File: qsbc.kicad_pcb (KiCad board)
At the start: 6 copper layers, 80 x 80 mm, 2 parts, among them U1 MIMX8MM6DVTLZAA, U3 MT40A1G16KD-062E

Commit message: misc work, usb sch done
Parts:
- added C1: 0.22uF, Capacitor_SMD:C_0201_0603Metric, F.Cu at (119.7, 123.8)
- added C10: 4.7uF, Capacitor_SMD:C_0402_1005Metric, F.Cu at (122.8, 121.9)
- added C11: 4.7uF, Capacitor_SMD:C_0402_1005Metric, F.Cu at (125.6, 121.7)
- added C12: 0.01uF, Capacitor_SMD:C_0201_0603Metric, F.Cu at (134.4, 115.7)
- added C13: 2.2uF, Capacitor_SMD:C_0402_1005Metric, F.Cu at (81.5, 124.2)
- added C14: 2.2uF, Capacitor_SMD:C_0402_1005Metric, F.Cu at (97.5, 112.0)
- added C15: 2.2uF, Capacitor_SMD:C_0402_1005Metric, F.Cu at (78.7, 124.0)
- added C16: 4.7uF, Capacitor_SMD:C_0402_1005Metric, F.Cu at (90.8, 120.1)
- added C17: 4.7uF, Capacitor_SMD:C_0402_1005Metric, F.Cu at (90.7, 122.1)
- added C18: 4.7uF, Capacitor_SMD:C_0402_1005Metric, F.Cu at (93.9, 115.1)
- added C2: 4.7uF, Capacitor_SMD:C_0402_1005Metric, F.Cu at (125.6, 123.7)
- added C27: 1uF, Capacitor_SMD:C_0402_1005Metric, F.Cu at (90.1, 124.0)
- added C28: 1uF, Capacitor_SMD:C_0402_1005Metric, F.Cu at (97.5, 114.0)
- added C29: 4.7uF, Capacitor_SMD:C_0402_1005Metric, F.Cu at (96.8, 116.0)
- added C3: 4.7uF, Capacitor_SMD:C_0402_1005Metric, F.Cu at (131.7, 115.8)
- added C30: 4.7uF, Capacitor_SMD:C_0402_1005Metric, F.Cu at (87.3, 124.2)
- added C31: 4.7uF, Capacitor_SMD:C_0402_1005Metric, F.Cu at (87.8, 121.2)
- added C32: 4.7uF, Capacitor_SMD:C_0402_1005Metric, F.Cu at (93.7, 119.0)
- added C4: 4.7uF, Capacitor_SMD:C_0402_1005Metric, F.Cu at (131.7, 117.8)
- added C45: 18pF, Capacitor_SMD:C_0402_1005Metric, F.Cu at (100.4, 112.0)
- added C47: 18pF, Capacitor_SMD:C_0402_1005Metric, F.Cu at (93.9, 117.0)
- added C48: 1uF, Capacitor_SMD:C_0402_1005Metric, F.Cu at (90.8, 118.1)
- added C49: 1uF, Capacitor_SMD:C_0402_1005Metric, F.Cu at (84.4, 124.2)
- added C5: 4.7uF, Capacitor_SMD:C_0402_1005Metric, F.Cu at (126.0, 117.8)
- added C50: 0.1uF, Capacitor_SMD:C_0402_1005Metric, F.Cu at (144.6, 173.0)
- added C51: 0.1uF, Capacitor_SMD:C_0402_1005Metric, F.Cu at (154.0, 167.7)
- added C52: 1nF, Capacitor_SMD:C_0603_1608Metric, F.Cu at (150.5, 168.0)
- added C53: 0.1uF, Capacitor_SMD:C_0402_1005Metric, F.Cu at (155.3, 164.5)
- added C54: 10uF, Capacitor_SMD:C_0603_1608Metric, F.Cu at (136.4, 173.3)
- added C6: 1uF, Capacitor_SMD:C_0402_1005Metric, F.Cu at (128.9, 115.8)
- added C7: 1uF, Capacitor_SMD:C_0402_1005Metric, F.Cu at (128.7, 119.7)
- added C8: 4.7uF, Capacitor_SMD:C_0402_1005Metric, F.Cu at (125.8, 119.7)
- added C9: 4.7uF, Capacitor_SMD:C_0402_1005Metric, F.Cu at (128.8, 117.8)
- added FB1: FerriteBead, Resistor_SMD:R_0603_1608Metric, F.Cu at (140.4, 173.2)
- added J1: USB_C_Receptacle_USB2.0, Connector_USB:USB_C_Receptacle_HRO_TYPE-C-31-M-12, F.Cu at (136.1, 65.1)
- added J2: USB_C_Receptacle_USB2.0, Connector_USB:USB_C_Receptacle_HRO_TYPE-C-31-M-12, F.Cu at (135.3, 132.8)
- added J3: USB_C_Receptacle_USB2.0, Connector_USB:USB_C_Receptacle_HRO_TYPE-C-31-M-12, F.Cu at (153.2, 132.5)
- added J4: ARJM11D7-502-AB-EW2, qsbc:ARJM11D7-502-AB-EW2, F.Cu at (175.9, 119.7)
- added J7: USB_C_Receptacle_USB2.0, Connector_USB:USB_C_Receptacle_HRO_TYPE-C-31-M-12, F.Cu at (117.3, 133.2)
- added R12: 100K, Resistor_SMD:R_0402_1005Metric, F.Cu at (138.8, 175.5)
- added R13: 100K, Resistor_SMD:R_0402_1005Metric, F.Cu at (150.0, 170.2)
- added R14: 100K, Resistor_SMD:R_0402_1005Metric, F.Cu at (135.9, 175.5)
- added R17: 30K, Resistor_SMD:R_0402_1005Metric, F.Cu at (155.3, 162.5)
- added R18: 1M, Resistor_SMD:R_0402_1005Metric, F.Cu at (141.7, 175.5)
- added R3: 43R, Resistor_SMD:R_0201_0603Metric, F.Cu at (122.6, 123.7)
- added R4: 43R, Resistor_SMD:R_0201_0603Metric, F.Cu at (131.3, 119.6)
- added R5: 43R, Resistor_SMD:R_0201_0603Metric, F.Cu at (128.3, 121.6)
- added R6: 10K, Resistor_SMD:R_0402_1005Metric, F.Cu at (119.9, 121.9)
- added R7: 1K, Resistor_SMD:R_0402_1005Metric, F.Cu at (126.0, 115.8)
- added R8: 1K, Resistor_SMD:R_0402_1005Metric, F.Cu at (122.9, 118.8)
- added TP1: TestPoint, TestPoint:TestPoint_Pad_D1.0mm, F.Cu at (120.0, 116.3)
- added TP10: TestPoint, TestPoint:TestPoint_Pad_D1.0mm, F.Cu at (82.4, 112.6)
- added TP11: TestPoint, TestPoint:TestPoint_Pad_D1.0mm, F.Cu at (84.8, 115.6)
- added TP12: TestPoint, TestPoint:TestPoint_Pad_D1.0mm, F.Cu at (85.4, 112.6)
- added TP13: TestPoint, TestPoint:TestPoint_Pad_D1.0mm, F.Cu at (84.8, 118.7)
- added TP14: TestPoint, TestPoint:TestPoint_Pad_D1.0mm, F.Cu at (78.7, 118.5)
- added TP15: TestPoint, TestPoint:TestPoint_Pad_D1.0mm, F.Cu at (78.7, 115.4)
- added TP16: TestPoint, TestPoint:TestPoint_Pad_D1.0mm, F.Cu at (84.8, 121.7)
- added TP17: TestPoint, TestPoint:TestPoint_Pad_D1.0mm, F.Cu at (87.9, 118.7)
- added TP18: TestPoint, TestPoint:TestPoint_Pad_D1.0mm, F.Cu at (87.9, 115.6)
- added TP19: TestPoint, TestPoint:TestPoint_Pad_D1.0mm, F.Cu at (78.7, 121.5)
- added TP2: TestPoint, TestPoint:TestPoint_Pad_D1.0mm, F.Cu at (120.0, 119.4)
- added TP20: TestPoint, TestPoint:TestPoint_Pad_D1.0mm, F.Cu at (88.5, 112.6)
- added TP3: TestPoint, TestPoint:TestPoint_Pad_D1.0mm, F.Cu at (123.0, 116.3)
- added TP4: TestPoint, TestPoint:TestPoint_Pad_D1.0mm, F.Cu at (94.6, 112.6)
- added TP5: TestPoint, TestPoint:TestPoint_Pad_D1.0mm, F.Cu at (90.9, 115.6)
- added TP6: TestPoint, TestPoint:TestPoint_Pad_D1.0mm, F.Cu at (91.5, 112.6)
- added TP7: TestPoint, TestPoint:TestPoint_Pad_D1.0mm, F.Cu at (81.8, 115.6)
- added TP8: TestPoint, TestPoint:TestPoint_Pad_D1.0mm, F.Cu at (81.8, 121.7)
- added TP9: TestPoint, TestPoint:TestPoint_Pad_D1.0mm, F.Cu at (81.8, 118.7)
- added U10: TUSB320LI, Package_DFN_QFN:Texas_X2QFN-12_1.6x1.6mm_P0.4mm, F.Cu at (138.3, 151.9)
- added U11: TUSB320, Package_DFN_QFN:Texas_X2QFN-12_1.6x1.6mm_P0.4mm, F.Cu at (142.1, 151.9)
- added U12: TPD4EUSB30, Package_SON:USON-10_2.5x1.0mm_P0.5mm, F.Cu at (132.1, 152.0)
- added U13: TPD4EUSB30, Package_SON:USON-10_2.5x1.0mm_P0.5mm, F.Cu at (178.2, 112.0)
- added U14: TPD4EUSB30, Package_SON:USON-10_2.5x1.0mm_P0.5mm, F.Cu at (174.2, 112.0)
- added U15: W25Q32JVZP, Package_SON:WSON-8-1EP_6x5mm_P1.27mm_EP3.4x4.3mm, F.Cu at (167.0, 81.8)
- added U16: BD71847MWV, qsbc:UQFN56BV7070, F.Cu at (119.5, 114.7)
- added U17: CH343P, Package_DFN_QFN:QFN-16-1EP_3x3mm_P0.5mm_EP1.45x1.45mm_ThermalVias, F.Cu at (116.2, 130.1)
- added U18: RTL8211F, Package_DFN_QFN:QFN-40-1EP_5x5mm_P0.4mm_EP3.6x3.6mm_ThermalVias, F.Cu at (172.1, 105.2)
- added U19: NX5P3363, Package_CSP:WLCSP-16_2.225x2.17mm_P0.5mm, F.Cu at (151.2, 164.1)
- added U4: TPD4EUSB30, Package_SON:USON-10_2.5x1.0mm_P0.5mm, F.Cu at (133.0, 174.0)
- added U5: CH343P, Package_DFN_QFN:QFN-16-1EP_3x3mm_P0.5mm_EP1.45x1.45mm_ThermalVias, F.Cu at (145.9, 169.4)
- added U7: TPD4EUSB30, Package_SON:USON-10_2.5x1.0mm_P0.5mm, F.Cu at (134.9, 152.0)
- added U9: NX5P3363, Package_CSP:WLCSP-16_2.225x2.17mm_P0.5mm, F.Cu at (145.9, 164.1)
- added Y1: Crystal, Crystal:Crystal_SMD_2012-2Pin_2.0x1.2mm, F.Cu at (79.0, 112.5)
- moved U3 37.6 mm to (125.5, 105.9)
- moved U1 33.4 mm to (147.9, 98.9)
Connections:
- U1 pad A22: unconnected-(U1-PadA22) -> /USB/USB1_DN
- U1 pad A23: unconnected-(U1-PadA23) -> /USB/USB2_DN
- U1 pad B22: unconnected-(U1-PadB22) -> /USB/USB1_DP
- U1 pad B23: unconnected-(U1-PadB23) -> /USB/USB2_DP
- U1 pad D22: unconnected-(U1-PadD22) -> /USB/USB1_ID
- U1 pad D23: unconnected-(U1-PadD23) -> /USB/USB2_ID
- U1 pad P1: /DDR/DRAM_VREF -> /DDR/PHY_VREF
- U3 pad A2: unconnected-(U3-PadA2) -> GND
- U3 pad A8: unconnected-(U3-PadA8) -> GND
- U3 pad B2: unconnected-(U3-PadB2) -> GND
- U3 pad C9: unconnected-(U3-PadC9) -> GND
- U3 pad D2: unconnected-(U3-PadD2) -> GND
- U3 pad D8: unconnected-(U3-PadD8) -> GND
- U3 pad E1: unconnected-(U3-PadE1) -> GND
- U3 pad E3: unconnected-(U3-PadE3) -> GND
- U3 pad E8: unconnected-(U3-PadE8) -> GND
- U3 pad E9: unconnected-(U3-PadE9) -> GND
- U3 pad F1: unconnected-(U3-PadF1) -> GND
- U3 pad G8: unconnected-(U3-PadG8) -> GND
- U3 pad H1: unconnected-(U3-PadH1) -> GND
- U3 pad H9: unconnected-(U3-PadH9) -> GND
- U3 pad K1: unconnected-(U3-PadK1) -> GND
- U3 pad K9: unconnected-(U3-PadK9) -> GND
- U3 pad M9: unconnected-(U3-PadM9) -> GND
- U3 pad N1: unconnected-(U3-PadN1) -> GND
- U3 pad T1: unconnected-(U3-PadT1) -> GND
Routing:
- net /DDR/DRAM_A13: track 0.00 -> 3.56 mm
- net /DDR/DRAM_A10: track 0.00 -> 2.77 mm

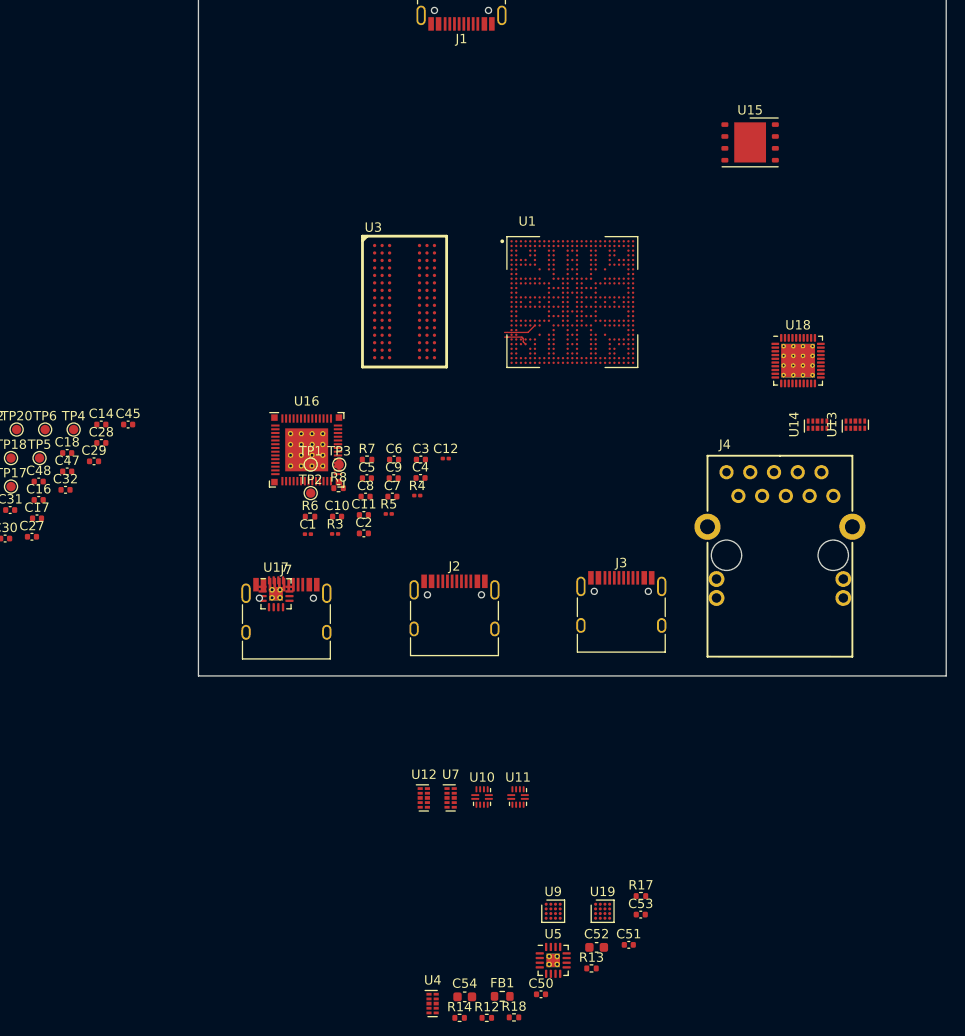
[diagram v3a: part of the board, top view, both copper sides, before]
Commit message: enet sch done, other misc sch work
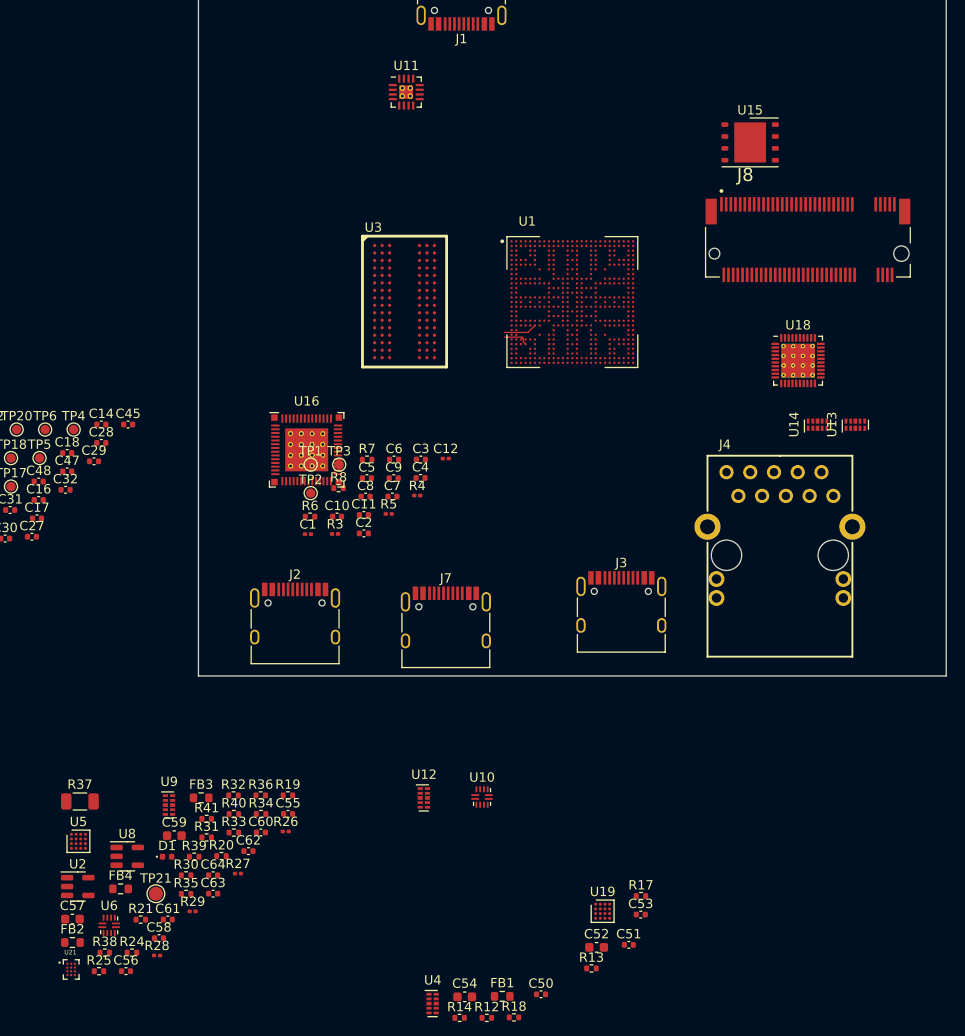
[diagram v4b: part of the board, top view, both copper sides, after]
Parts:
- removed U17: CH343P, Package_DFN_QFN:QFN-16-1EP_3x3mm_P0.5mm_EP1.45x1.45mm_ThermalVias
- removed U7: TPD4EUSB30, Package_SON:USON-10_2.5x1.0mm_P0.5mm
- added C55: 0.1uF, Capacitor_SMD:C_0402_1005Metric, F.Cu at (117.5, 153.7)
- added C56: 0.1uF, Capacitor_SMD:C_0402_1005Metric, F.Cu at (100.2, 170.5)
- added C57: 1nF, Capacitor_SMD:C_0603_1608Metric, F.Cu at (94.5, 164.9)
- added C58: 0.1uF, Capacitor_SMD:C_0402_1005Metric, F.Cu at (103.7, 167.0)
- added C59: 10uF, Capacitor_SMD:C_0603_1608Metric, F.Cu at (105.4, 156.0)
- added C60: 0.22uF, Capacitor_SMD:C_0402_1005Metric, F.Cu at (114.6, 155.7)
- added C61: 0.22uF, Capacitor_SMD:C_0402_1005Metric, F.Cu at (104.7, 165.0)
- added C62: 1uF, Capacitor_SMD:C_0402_1005Metric, F.Cu at (113.3, 157.7)
- added C63: 0.1uF, Capacitor_SMD:C_0402_1005Metric, F.Cu at (109.5, 162.2)
- added C64: 0.1uF, Capacitor_SMD:C_0402_1005Metric, F.Cu at (109.5, 160.2)
- added D1: LED YELLOW, LED_SMD:LED_0402_1005Metric, F.Cu at (104.6, 158.3)
- added FB2: FerriteBead, Resistor_SMD:R_0603_1608Metric, F.Cu at (94.5, 167.4)
- added FB3: FerriteBead, Resistor_SMD:R_0603_1608Metric, F.Cu at (108.2, 152.0)
- added FB4: FerriteBead, Resistor_SMD:R_0603_1608Metric, F.Cu at (99.6, 161.7)
- added J8: Bus_M.2_Socket_M, qsbc:1-2199230-6, F.Cu at (173.1, 93.7)
- added R19: 100K, Resistor_SMD:R_0402_1005Metric, F.Cu at (117.5, 151.7)
- added R20: 100K, Resistor_SMD:R_0402_1005Metric, F.Cu at (110.4, 158.2)
- added R21: 100K, Resistor_SMD:R_0402_1005Metric, F.Cu at (101.8, 165.0)
- added R24: 30K, Resistor_SMD:R_0402_1005Metric, F.Cu at (100.8, 168.5)
- added R25: 1M, Resistor_SMD:R_0402_1005Metric, F.Cu at (97.3, 170.5)
- added R26: 200R, Resistor_SMD:R_0201_0603Metric, F.Cu at (117.3, 155.6)
- added R27: 200R, Resistor_SMD:R_0201_0603Metric, F.Cu at (112.2, 160.1)
- added R28: 30K, Resistor_SMD:R_0201_0603Metric, F.Cu at (103.5, 168.8)
- added R29: 30K, Resistor_SMD:R_0201_0603Metric, F.Cu at (107.3, 164.1)
- added R30: 0R, Resistor_SMD:R_0402_1005Metric, F.Cu at (106.6, 160.3)
- added R31: 0R, Resistor_SMD:R_0402_1005Metric, F.Cu at (108.8, 156.2)
- added R32: 0R, Resistor_SMD:R_0402_1005Metric, F.Cu at (111.7, 151.7)
- added R33: 0R, Resistor_SMD:R_0402_1005Metric, F.Cu at (111.7, 155.7)
- added R34: 2.2K, Resistor_SMD:R_0402_1005Metric, F.Cu at (114.6, 153.7)
- added R35: 100K, Resistor_SMD:R_0402_1005Metric, F.Cu at (106.6, 162.2)
- added R36: 10K, Resistor_SMD:R_0402_1005Metric, F.Cu at (114.6, 151.7)
- added R37: 10m, Resistor_SMD:R_1206_3216Metric, F.Cu at (95.3, 152.4)
- added R38: 5.1K, Resistor_SMD:R_0402_1005Metric, F.Cu at (97.9, 168.5)
- added R39: 5.1K, Resistor_SMD:R_0402_1005Metric, F.Cu at (107.5, 158.3)
- added R40: 5.1K, Resistor_SMD:R_0402_1005Metric, F.Cu at (111.7, 153.7)
- added R41: 5.1K, Resistor_SMD:R_0402_1005Metric, F.Cu at (108.8, 154.2)
- added TP21: TestPoint, TestPoint:TestPoint_Pad_D1.5mm, F.Cu at (103.4, 162.2)
- added U2: 74LVC1G04, Package_TO_SOT_SMD:SOT-23-5, F.Cu at (95.0, 161.5)
- added U21: INA231, qsbc:DSBGA-12, F.Cu at (94.3, 170.3)
- added U6: TUSB320LI, Package_DFN_QFN:Texas_X2QFN-12_1.6x1.6mm_P0.4mm, F.Cu at (98.4, 165.6)
- added U8: 74LVC1G04, Package_TO_SOT_SMD:SOT-23-5, F.Cu at (100.3, 158.2)
- U11: value TUSB320 -> CH343P; footprint Package_DFN_QFN:Texas_X2QFN-12_1.6x1.6mm_P0.4mm -> Package_DFN_QFN:QFN-16-1EP_3x3mm_P0.5mm_EP1.45x1.45mm_ThermalVias
- U5: value CH343P -> NX5P3363; footprint Package_DFN_QFN:QFN-16-1EP_3x3mm_P0.5mm_EP1.45x1.45mm_ThermalVias -> Package_CSP:WLCSP-16_2.225x2.17mm_P0.5mm
- U9: value NX5P3363 -> TPD4EUSB30; footprint Package_CSP:WLCSP-16_2.225x2.17mm_P0.5mm -> Package_SON:USON-10_2.5x1.0mm_P0.5mm
- moved U11 76.4 mm to (130.2, 76.5)
- moved U5 52.4 mm to (95.1, 156.6)
- moved U9 42.6 mm to (104.8, 152.7)
- moved J7 17.1 mm to (134.4, 134.1)
- moved J2 17.1 mm to (118.3, 133.7)
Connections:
- net Net-(J3-PadA4) renamed /USB/USB2_VBUS
- net Net-(J7-PadA4) renamed /USB/USB4_VBUS
- J1 pad A1: Net-(J1-PadA1) -> GND
- J1 pad A12: Net-(J1-PadA1) -> GND
- J1 pad A4: Net-(J1-PadA4) -> /USB/USB3_VBUS
- J1 pad A5: unconnected-(J1-PadA5) -> /USB/USB3_CC1
- J1 pad A9: Net-(J1-PadA4) -> /USB/USB3_VBUS
- J1 pad B1: Net-(J1-PadA1) -> GND
- J1 pad B12: Net-(J1-PadA1) -> GND
- J1 pad B4: Net-(J1-PadA4) -> /USB/USB3_VBUS
- J1 pad B5: unconnected-(J1-PadB5) -> /USB/USB3_CC2
- J1 pad B9: Net-(J1-PadA4) -> /USB/USB3_VBUS
- J1 pad S1: unconnected-(J1-PadS1) -> Net-(J1-PadS1)
- J2 pad A1: Net-(J2-PadA1) -> GND
- J2 pad A12: Net-(J2-PadA1) -> GND
- J2 pad A4: Net-(J2-PadA4) -> /USB/USB1_VBUS
- J2 pad A5: unconnected-(J2-PadA5) -> /USB/USB1_CC1
- J2 pad A9: Net-(J2-PadA4) -> /USB/USB1_VBUS
- J2 pad B1: Net-(J2-PadA1) -> GND
- J2 pad B12: Net-(J2-PadA1) -> GND
- J2 pad B4: Net-(J2-PadA4) -> /USB/USB1_VBUS
- J2 pad B5: unconnected-(J2-PadB5) -> /USB/USB1_CC2
- J2 pad B9: Net-(J2-PadA4) -> /USB/USB1_VBUS
- J2 pad S1: unconnected-(J2-PadS1) -> Net-(FB2-Pad1)
- J7 pad A1: Net-(J7-PadA1) -> GND
- J7 pad A12: Net-(J7-PadA1) -> GND
- J7 pad A5: unconnected-(J7-PadA5) -> /USB/USB4_CC1
- J7 pad B1: Net-(J7-PadA1) -> GND
- J7 pad B12: Net-(J7-PadA1) -> GND
- J7 pad B5: unconnected-(J7-PadB5) -> /USB/USB4_CC2
- J7 pad S1: unconnected-(J7-PadS1) -> Net-(FB4-Pad1)
- U1 pad E19: unconnected-(U1-PadE19) -> Net-(U1-PadE19)
- U1 pad E22: unconnected-(U1-PadE22) -> Net-(U1-PadE22)
- U1 pad F22: unconnected-(U1-PadF22) -> Net-(U1-PadF22)
- U1 pad F23: unconnected-(U1-PadF23) -> Net-(U1-PadF23)
- U11 pad 1: unconnected-(U11-Pad1) -> GND
- U11 pad 10: unconnected-(U11-Pad10) -> Net-(R36-Pad1)
- U11 pad 12: unconnected-(U11-Pad12) -> Net-(R34-Pad2)
- U11 pad 2: unconnected-(U11-Pad2) -> GND
- U11 pad 3: unconnected-(U11-Pad3) -> /USB/VDD_3.3V
- U11 pad 4: unconnected-(U11-Pad4) -> Net-(R30-Pad2)
- U11 pad 5: unconnected-(U11-Pad5) -> Net-(R31-Pad2)
- U11 pad 6: unconnected-(U11-Pad6) -> /USB/VDD_3.3V
- U11 pad 7: unconnected-(U11-Pad7) -> /USB/USB3_DP
- U11 pad 8: unconnected-(U11-Pad8) -> /USB/USB3_DN
- U11 pad 9: unconnected-(U11-Pad9) -> /USB/USB3_VBUS
- U4 pad 1: Net-(U4-Pad1) -> unconnected-(U4-Pad1)
- U4 pad 10: Net-(U4-Pad1) -> unconnected-(U4-Pad1)
- U4 pad 2: Net-(U4-Pad2) -> unconnected-(U4-Pad2)
- U4 pad 3: Net-(U4-Pad3) -> GND
- U4 pad 4: Net-(U4-Pad4) -> /USB/USB3_DP
- U4 pad 5: Net-(U4-Pad5) -> /USB/USB3_DN
- U4 pad 6: Net-(U4-Pad5) -> /USB/USB3_DN
- U4 pad 7: Net-(U4-Pad4) -> /USB/USB3_DP
- U4 pad 8: Net-(U4-Pad3) -> GND
- U4 pad 9: Net-(U4-Pad2) -> unconnected-(U4-Pad2)
